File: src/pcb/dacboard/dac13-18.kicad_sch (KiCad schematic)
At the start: 18 parts, among them U34 AD8676xR, U35 AD8676xR, U36 AD8676xR, U37 AD8676xR, U38 AD5791BRUZ, U39 AD5791BRUZ, U40 AD5791BRUZ, U41 AD5791BRUZ, U42 AD8676xR, U43 AD8676xR, U44 AD5791BRUZ, U45 AD5791BRUZ

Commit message: dacboard routing
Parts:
- C34, C35, C36, C37, C38, C39: value C -> 10uF; footprint (none) -> Capacitor_SMD:C_0603_1608Metric_Pad1.08x0.95mm_HandSolder
- U38, U39, U40, U41, U44, U45: footprint RU_20_ADI -> Package_SO:TSSOP-20_4.4x6.5mm_P0.65mm

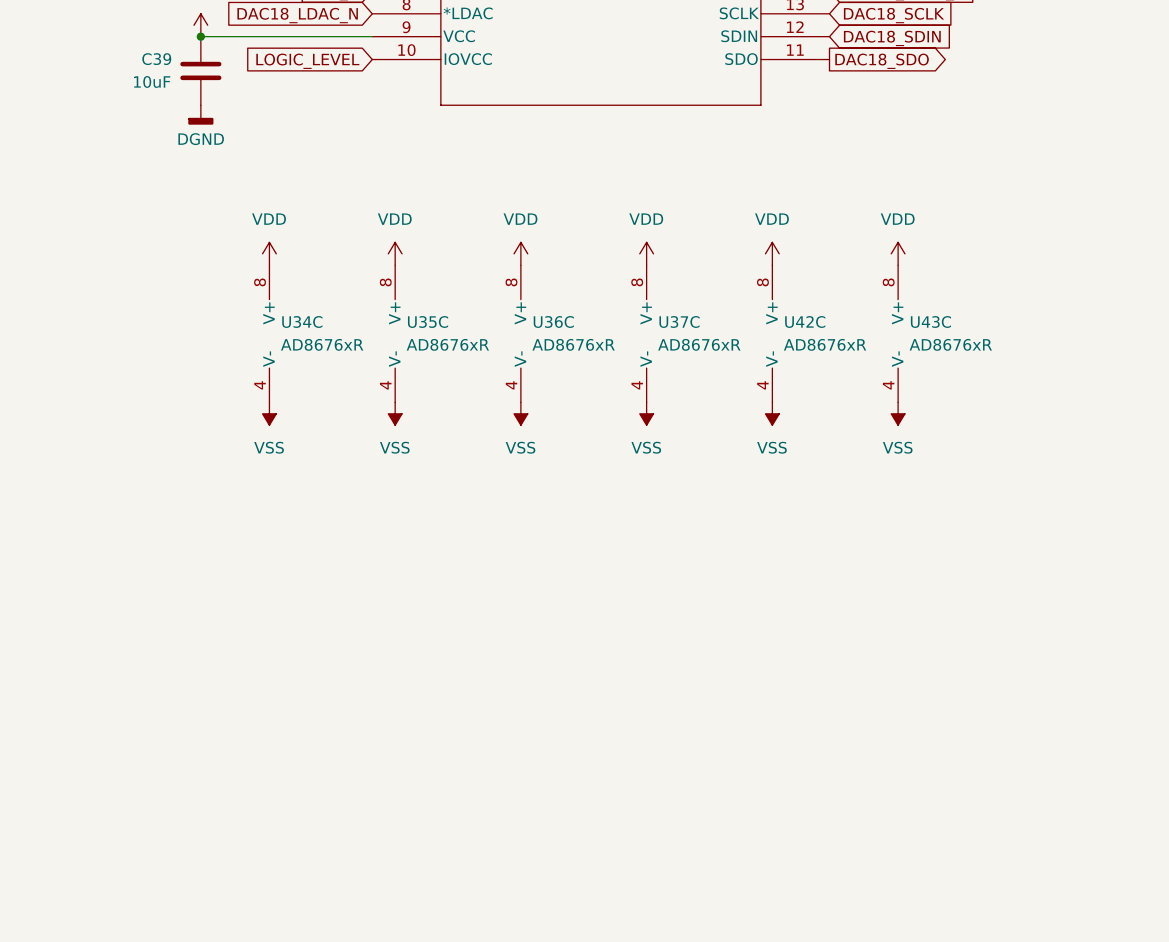
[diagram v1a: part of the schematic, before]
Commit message: adding more capacitors to analog side
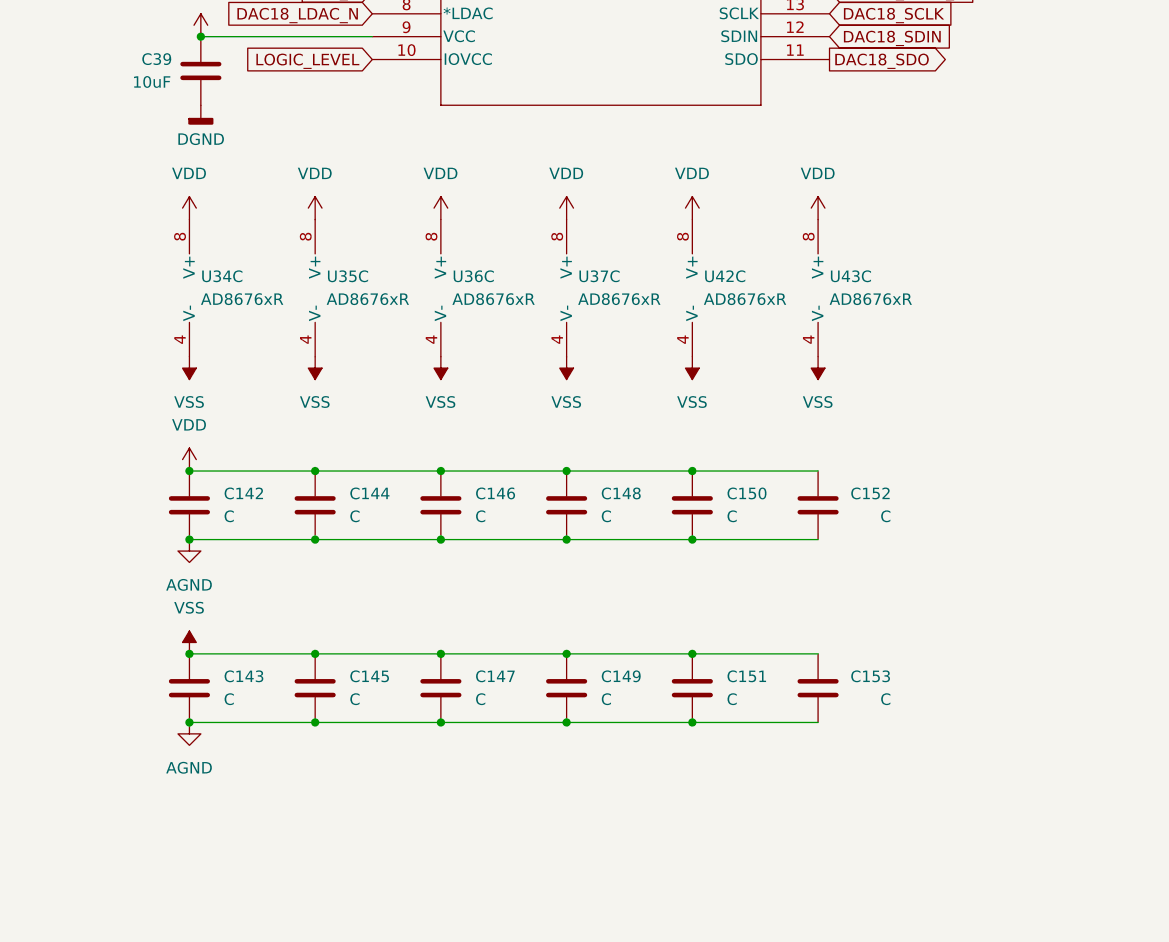
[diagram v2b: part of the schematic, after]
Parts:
- added C142, C143, C144, C145, C146, C147, C148, C149, C150, C151, C152, C153: C, Capacitor_SMD:C_0402_1005Metric_Pad0.74x0.62mm_HandSolder, symbol Device:C
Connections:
- net AGND: now also C142.2, C143.2, C144.2, C145.2, C146.2, C147.2, C148.2, C149.2, C150.2, C151.2, C152.2, C153.2
- net VDD: now also C142.1, C144.1, C146.1, C148.1, C150.1, C152.1
- net VSS: now also C143.1, C145.1, C147.1, C149.1, C151.1, C153.1
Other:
- moved on the sheet: U34C, U35C, U36C, U37C, U42C, U43C

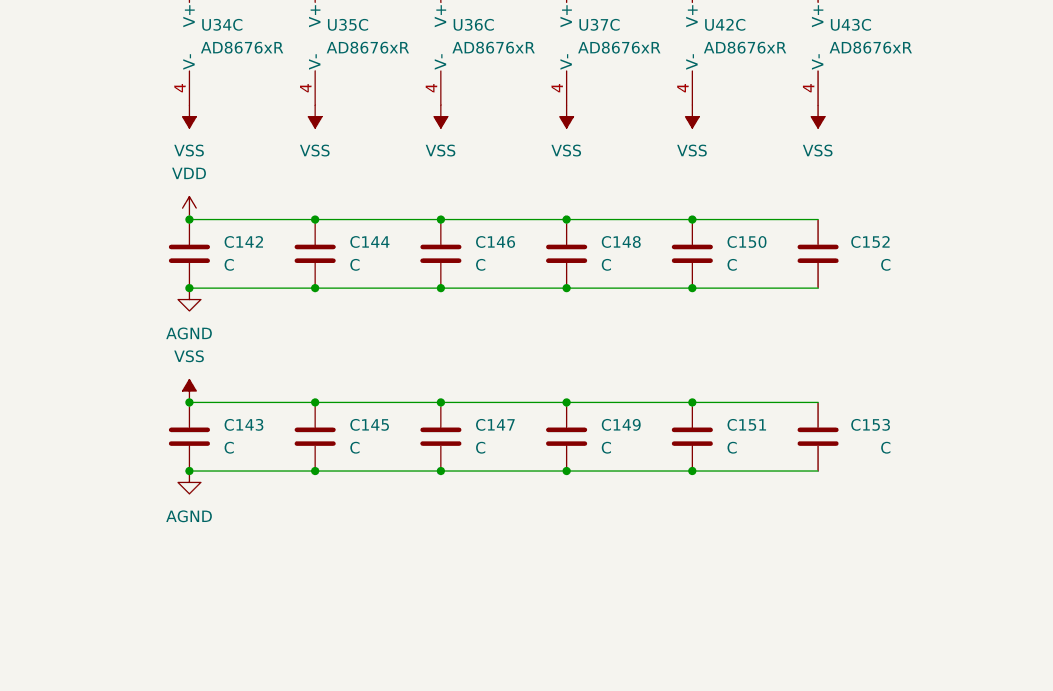
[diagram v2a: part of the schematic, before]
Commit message: more capacitors
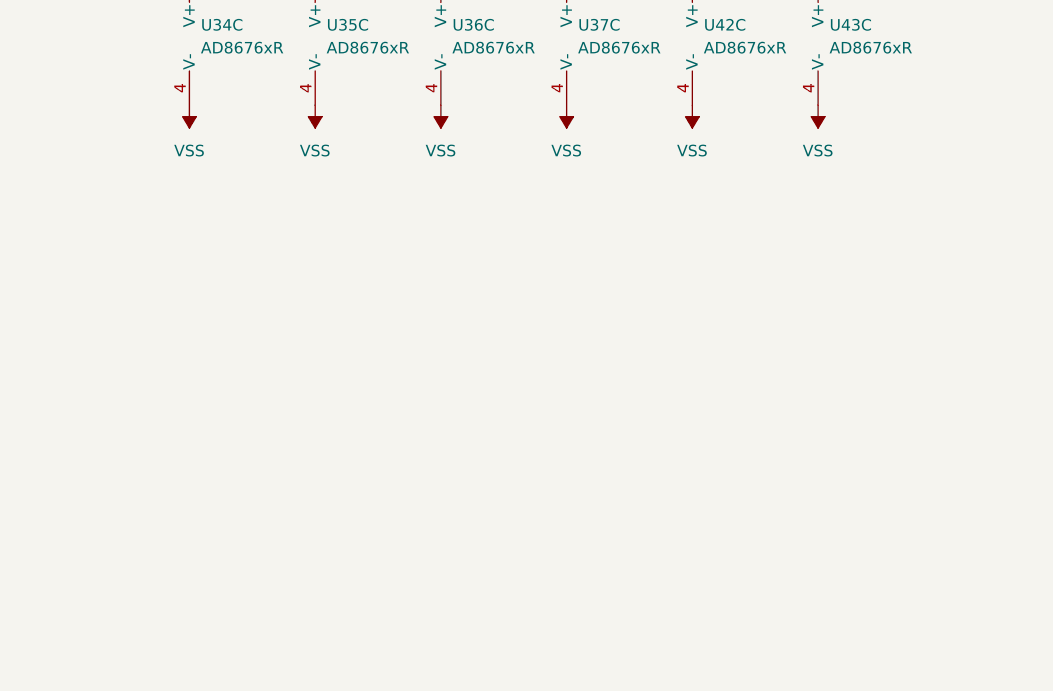
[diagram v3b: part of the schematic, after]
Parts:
- removed C142, C143, C144, C145, C146, C147, C148, C149, C150, C151, C152, C153: C, Capacitor_SMD:C_0402_1005Metric_Pad0.74x0.62mm_HandSolder, symbol Device:C

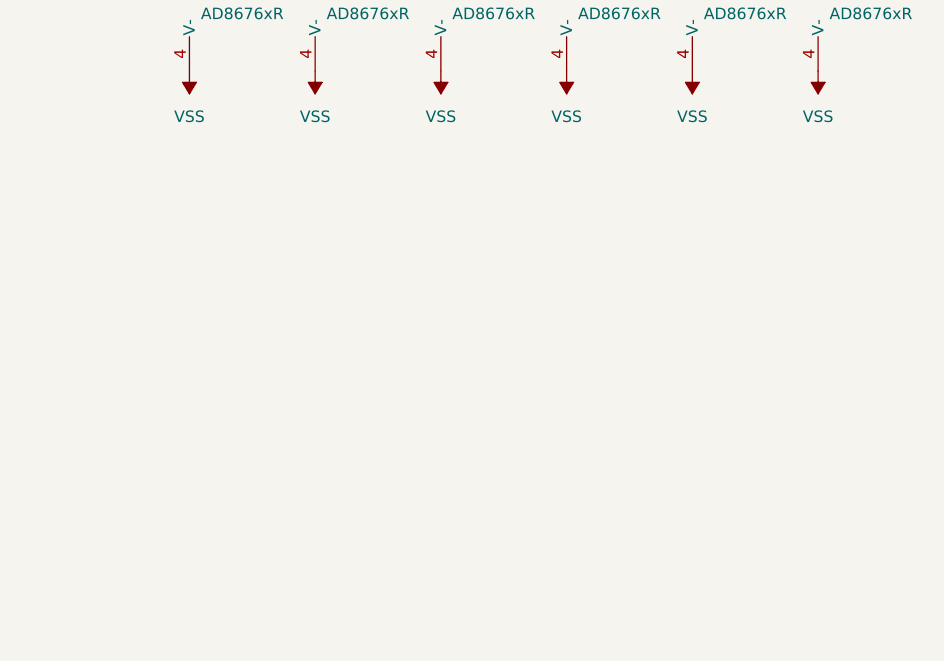
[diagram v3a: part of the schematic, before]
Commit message: got rid of all drc errors
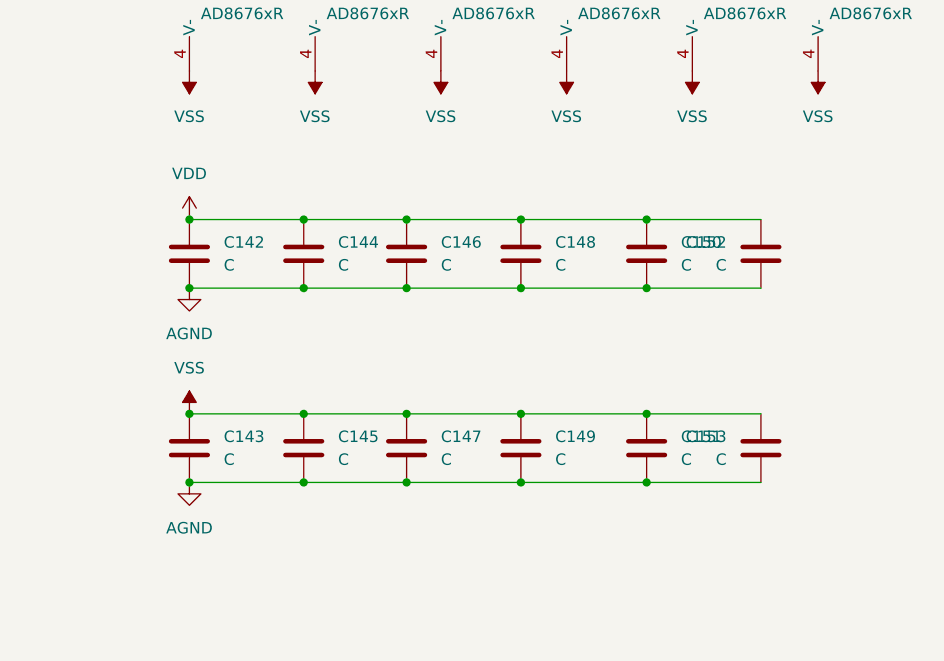
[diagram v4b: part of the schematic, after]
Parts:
- added C142, C143, C144, C145, C146, C147, C148, C149, C150, C151, C152, C153: C, Capacitor_SMD:C_0402_1005Metric_Pad0.74x0.62mm_HandSolder, symbol Device:C
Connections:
- net AGND: now also C142.2, C143.2, C144.2, C145.2, C146.2, C147.2, C148.2, C149.2, C150.2, C151.2, C152.2, C153.2
- net VDD: now also C142.1, C144.1, C146.1, C148.1, C150.1, C152.1
- net VSS: now also C143.1, C145.1, C147.1, C149.1, C151.1, C153.1
